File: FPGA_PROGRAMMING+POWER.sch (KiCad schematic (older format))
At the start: 28 parts, among them U301 iCE40-HX4K-TQ144, U302 25LC_EEPROM

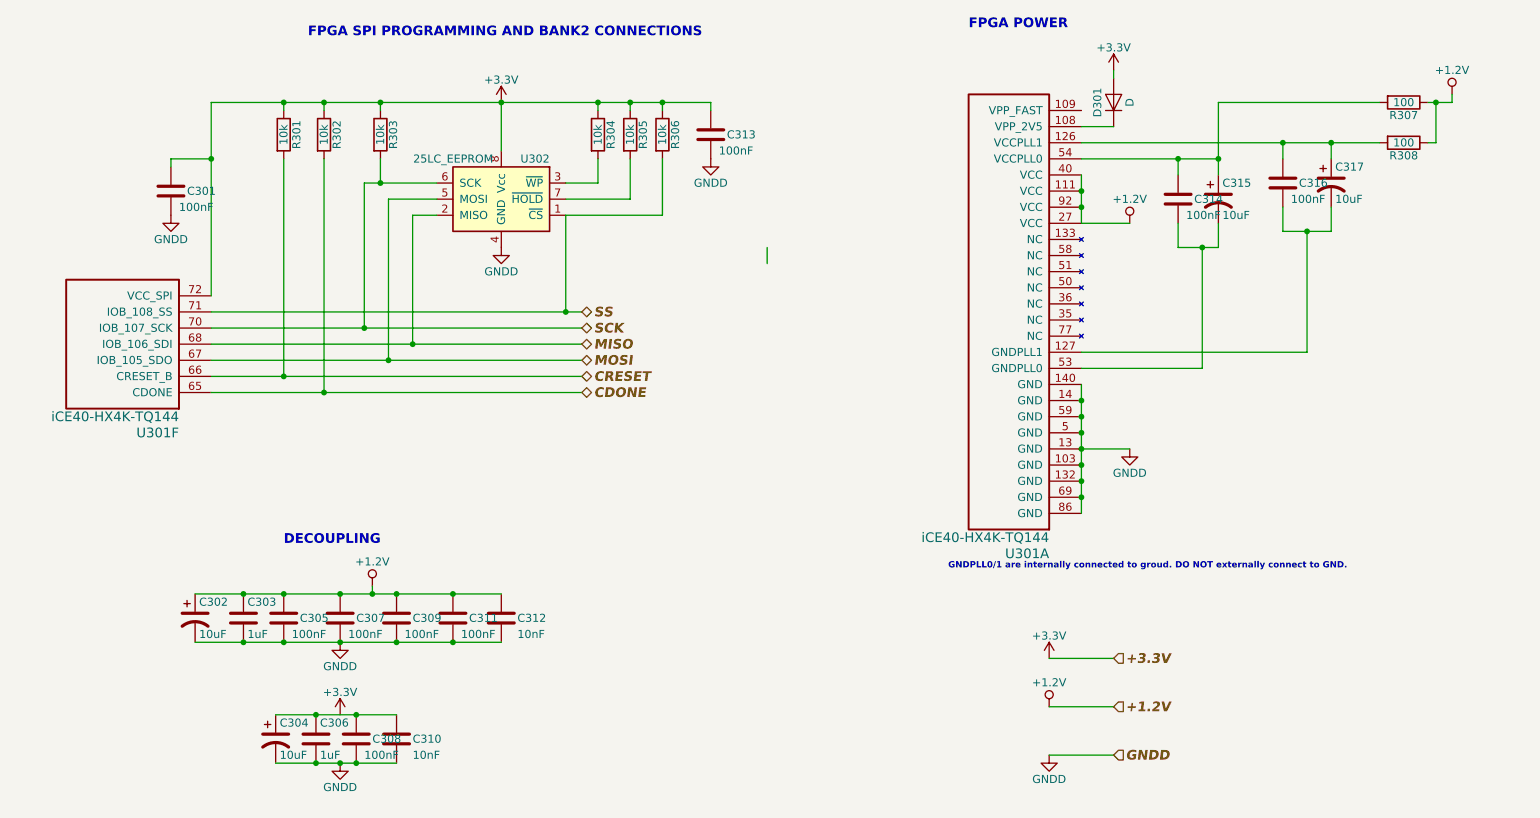
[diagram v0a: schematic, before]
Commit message: The schematic is now free of any ERC error. Not connected and power flags added. No more global power pins, hierarchical labels used for power connections. TODO list: -Check if all footpritns are already assigned. -Export a BOM list, and check if all part numbers are assigned. -Add leds and testpoints. -Make another branch, with the RAM connections to the left and right banks, so the ram could be located in the bottom layer and the FPGA in the top layer. -Reorder the connections of the current branch if necessary, do the placement of components and ground planes.
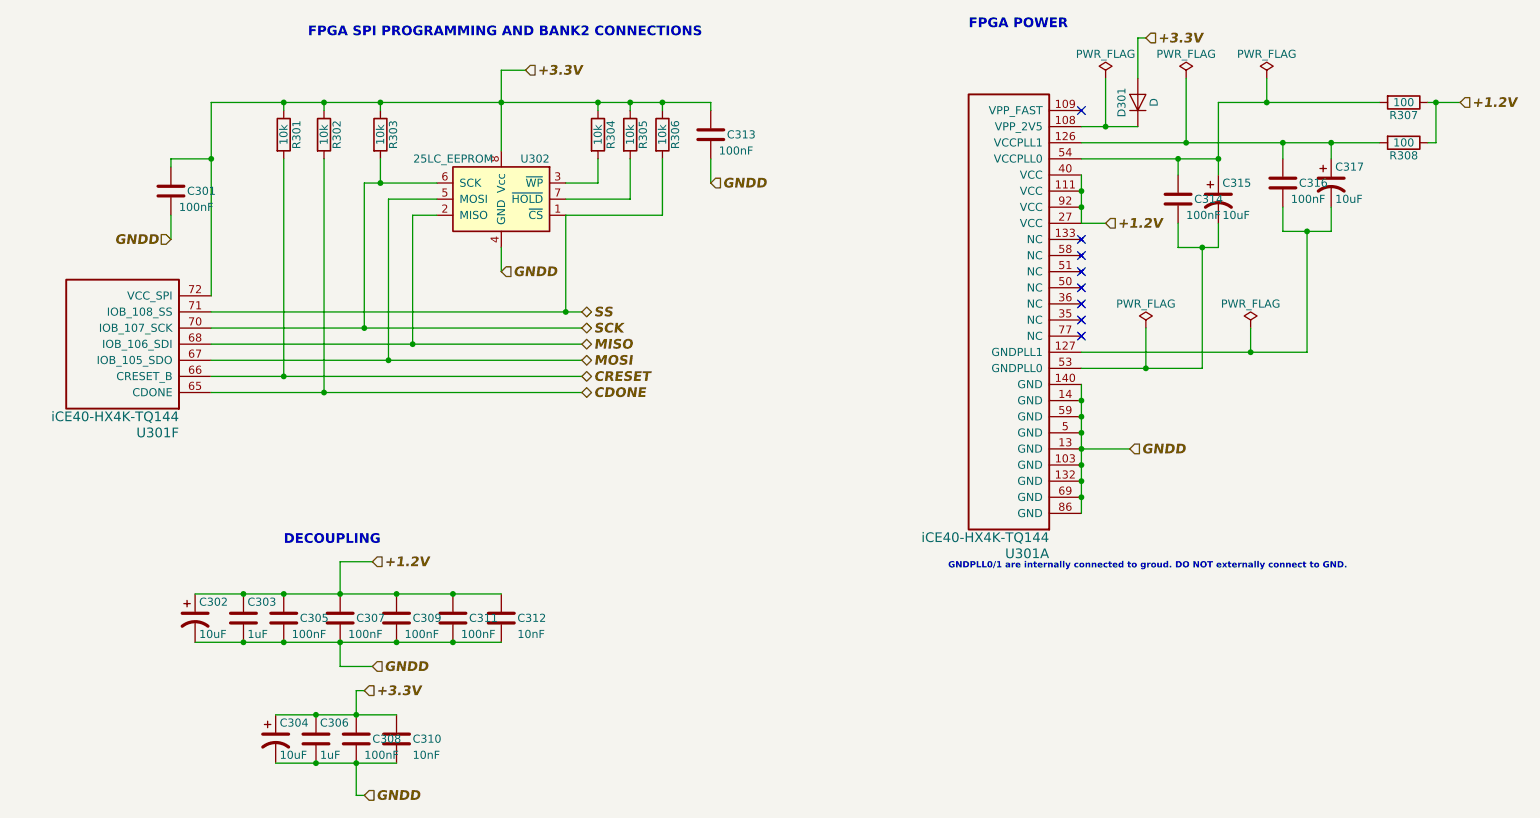
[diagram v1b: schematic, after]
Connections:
- net +3V3 is gone; now on net +3.3V: C301.1, C313.1, D301.2 (A), R301.1, R302.1, R303.1, R304.1, R305.1, R306.1, U301.72 (VCC_SPI), U302.8 (Vcc)
- net +3.3V: now reaches C304.1, C306.1, C308.1, C310.1
- no-connect marks 0 -> 8
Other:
- moved on the sheet: D301

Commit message: First netlist export
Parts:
- U301: footprint (none) -> Housings_QFP:LQFP-144_20x20mm_Pitch0.5mm
- U302: footprint (none) -> TO_SOT_Packages_SMD:SOT-23-8_Handsoldering
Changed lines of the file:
@@
 F 0 "U301" H 7750 4300 60  0000 L CNN
 F 1 "iCE40-HX4K-TQ144" H 7750 4200 60  0000 L CNN
-F 2 "" H 7550 4050 39  0001 C CNN
+F 2 "Housings_QFP:LQFP-144_20x20mm_Pitch0.5mm" H 7550 4050 39  0001 C CNN
 F 3 "" H 7550 4050 39  0001 C CNN
 	1    7550 4050
@@
 F 0 "U302" H 3650 2350 50  0000 L CNN
 F 1 "25LC_EEPROM" H 4000 2350 50  0000 L CNN
-F 2 "" H 3600 2050 50  0001 C CNN
+F 2 "TO_SOT_Packages_SMD:SOT-23-8_Handsoldering" H 3600 2050 50  0001 C CNN
 F 3 "" H 3600 2050 50  0001 C CNN
 	1    3950 2100
@@
 F 0 "U301" H 2350 3550 60  0000 L CNN
 F 1 "iCE40-HX4K-TQ144" H 2350 3450 60  0000 L CNN
-F 2 "" H 2150 3300 60  0001 C CNN
+F 2 "Housings_QFP:LQFP-144_20x20mm_Pitch0.5mm" H 2150 3300 60  0001 C CNN
 F 3 "" H 2150 3300 60  0001 C CNN
 	6    2150 3300
